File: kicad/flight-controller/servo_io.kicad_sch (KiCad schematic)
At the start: 2 parts, among them J7 RC Conn

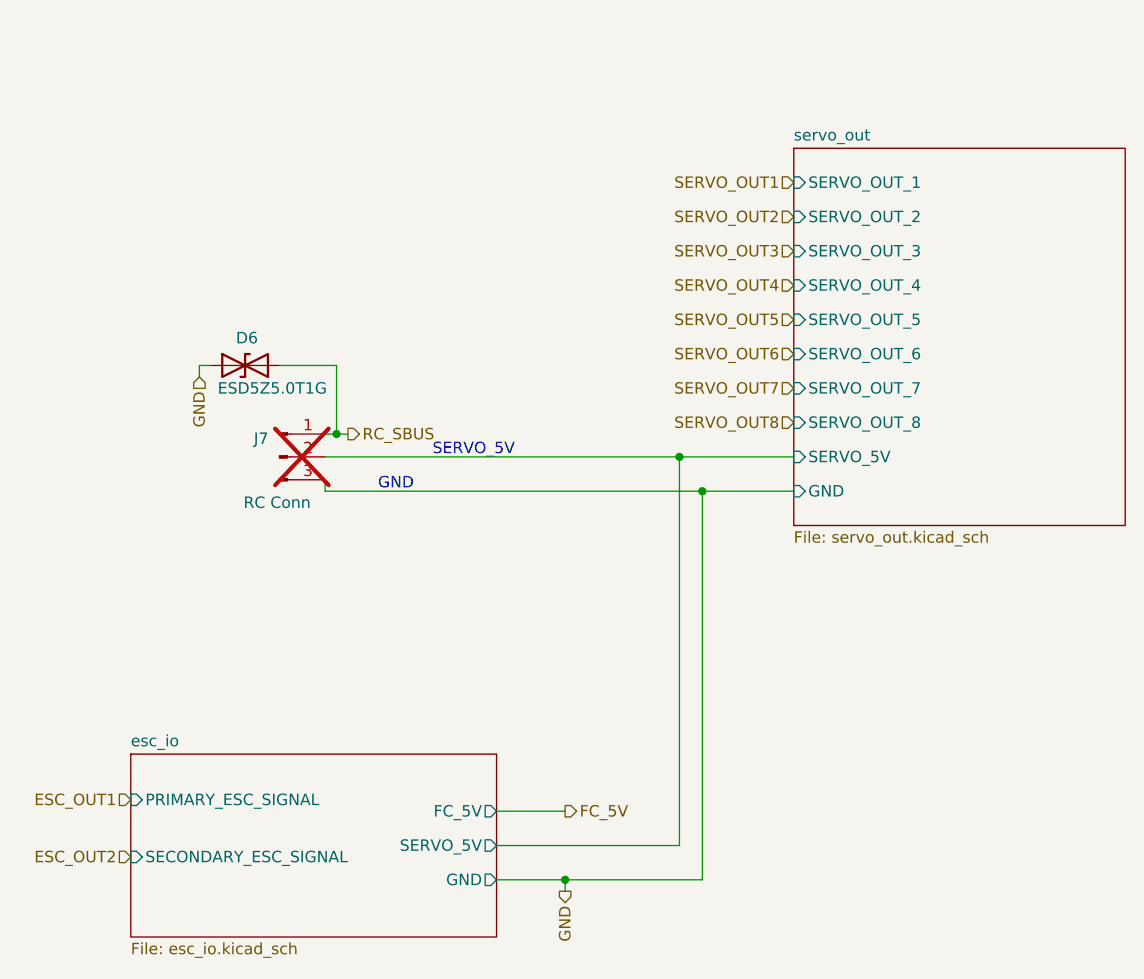
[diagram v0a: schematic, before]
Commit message: removed basestation code and v3.1 of fc pcb
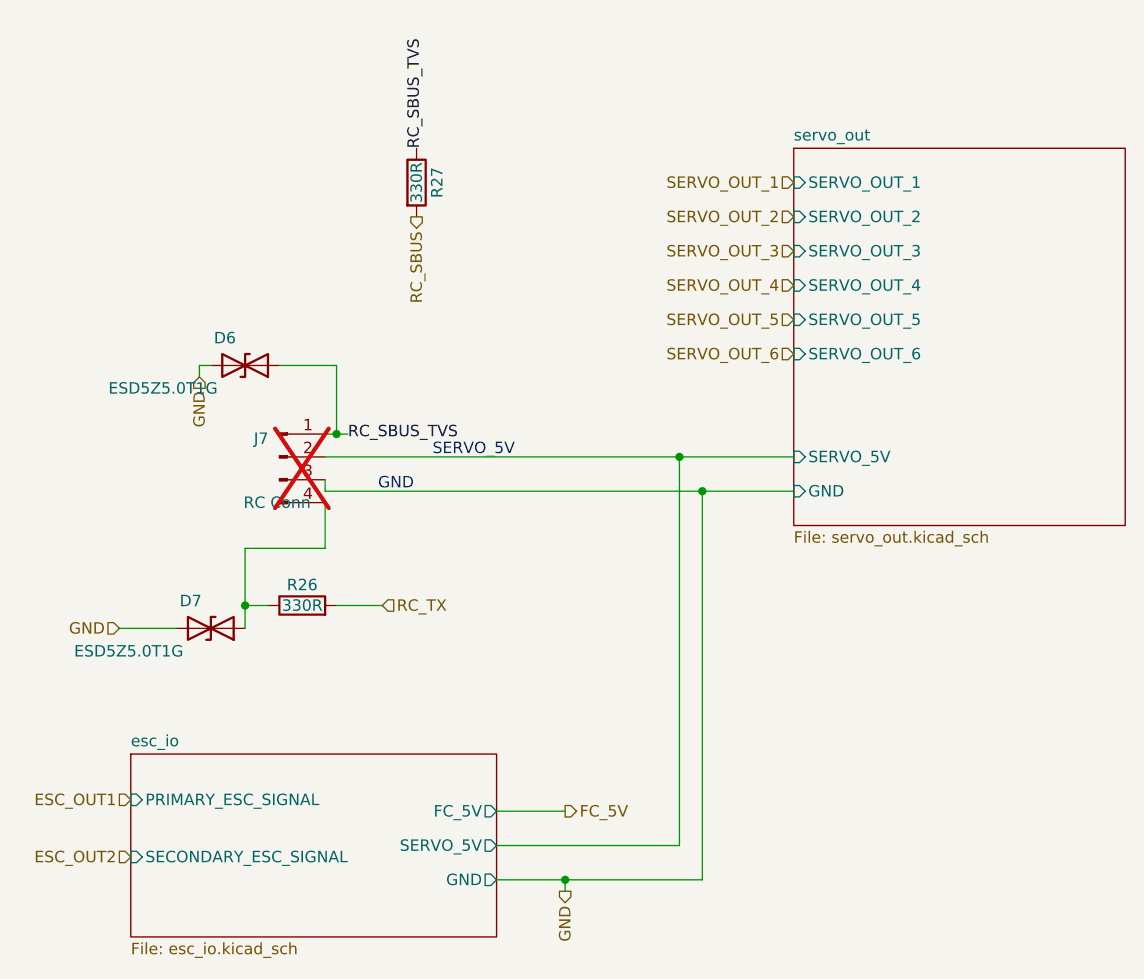
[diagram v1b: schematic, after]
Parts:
- added D7: ESD5Z5.0T1G, Diode_SMD:D_SOD-523, symbol Device:D_TVS
- added R26, R27: 330R, Resistor_SMD:R_0402_1005Metric, symbol Device:R
- J7: footprint Connector_Molex:Molex_KK-254_AE-6410-03A_1x03_P2.54mm_Vertical -> Connector_Molex:Molex_KK-254_AE-6410-04A_1x04_P2.54mm_Vertical; symbol Connector:Conn_01x03_Pin -> Connector:Conn_01x04_Pin; MPN (none) -> 0022232041; Manufacturer (none) -> Molex; now left out of the parts list
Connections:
- net GND: now also D6.2 (A2), D7.2 (A2); no longer D6.1 (A1)
- net RC_SBUS: now also R27.2; no longer D6.2 (A2), J7.1 (Pin_1)
- new net: D7.1 (A1), J7.4 (Pin_4), R26.1
- new net RC_SBUS_TVS: D6.1 (A1), J7.1 (Pin_1), R27.1
- new net RC_TX: R26.2
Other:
- sheet servo_out ports: added none; removed SERVO_OUT_7, SERVO_OUT_8
- moved on the sheet: D6

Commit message: Kicad FC v3.1 complete, Mission Controller and UWB boards v1 complete, firmware v2 complete!
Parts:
- R26, R27: LCSC Part (none) -> C25104
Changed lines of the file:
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@@
+			)
+		)
+		(property "LCSC Part" "C25104"
+			(at 109.22 58.42 0)
+			(hide yes)
+			(show_name no)
+			(do_not_autoplace no)
+			(effects
+				(font
+					(size 1.27 1.27)
+				)
 			)
 		)
@@
 			(at 96.52 105.41 0)
 			(hide yes)
+			(show_name no)
+			(do_not_autoplace no)
+			(effects
+				(font
+					(size 1.27 1.27)
+				)
+			)
+		)
+		(property "LCSC Part" "C25104"
+			(at 96.52 105.41 0)
+			(hide yes)
